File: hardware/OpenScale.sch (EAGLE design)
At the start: 58 parts, among them U1 HX711, U3 TMP102, U4 ATMEGA328P_TQFP, U5 MIC52055-5V, U6 FT231X, Y2 16MHZ

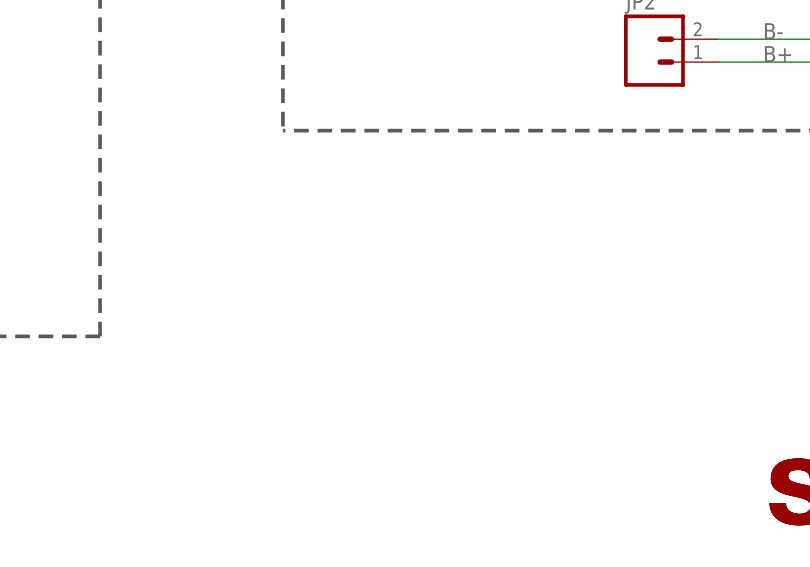
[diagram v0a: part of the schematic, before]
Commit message: Update file names. Remove stat LED blink delay.
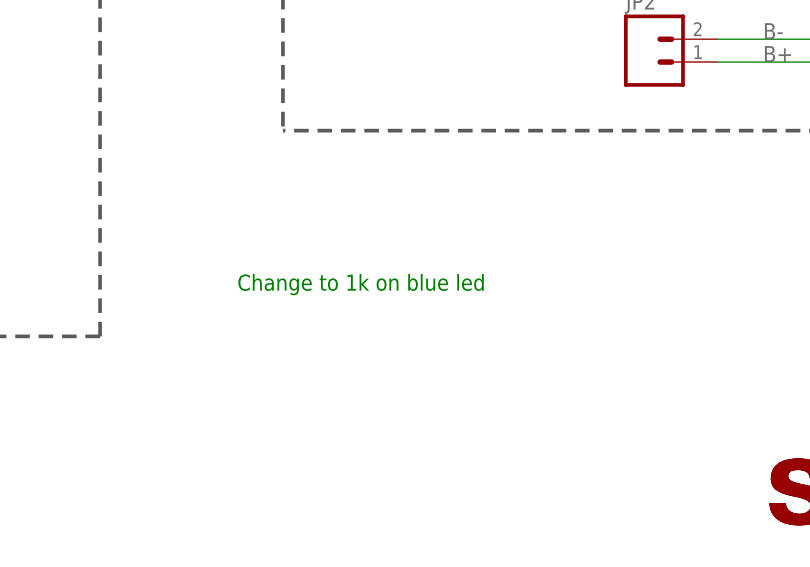
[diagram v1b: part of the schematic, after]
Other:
- note added: "Change to 1k on blue led"
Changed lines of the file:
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@@
 <text x="134.62" y="121.92" size="1.778" layer="97">Optional External
 Serial Interface</text>
+<text x="182.88" y="33.02" size="1.778" layer="91">Change to 1k on blue led</text>
 </plain>
 <instances>

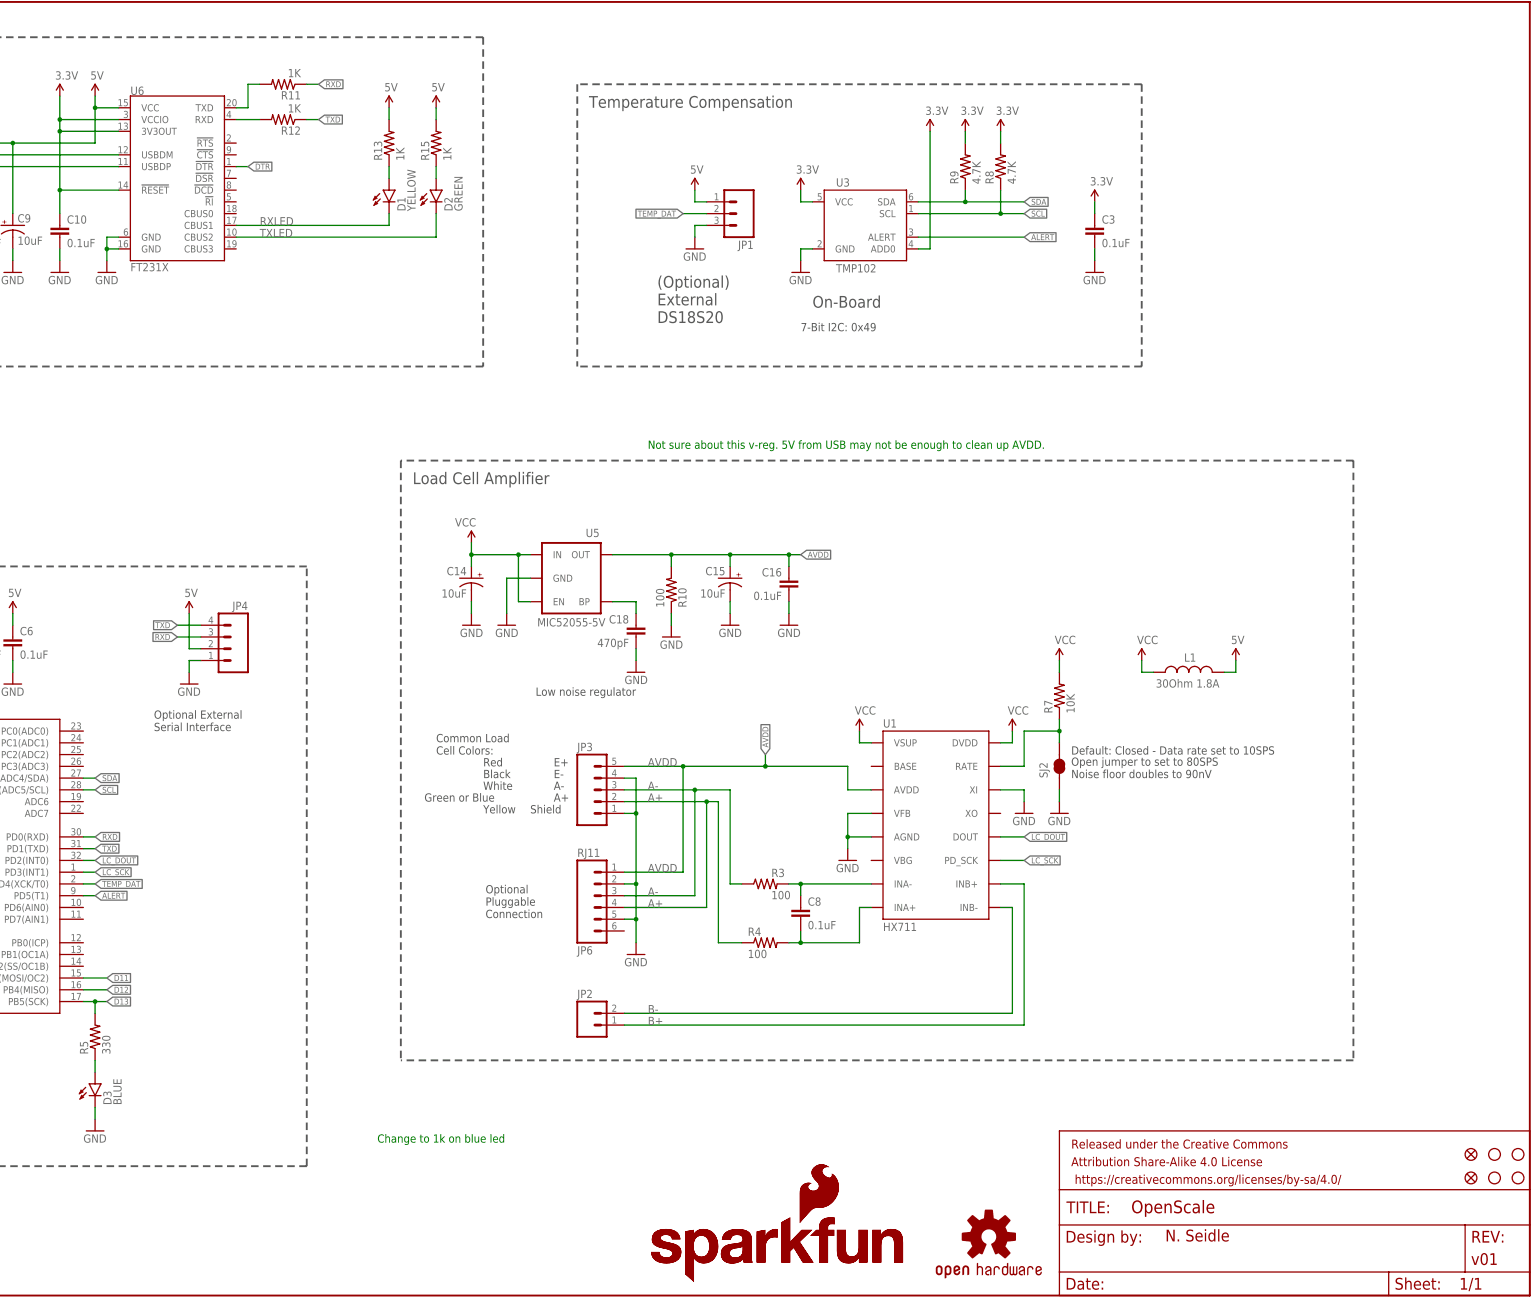
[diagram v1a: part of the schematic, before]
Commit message: Lots of changes. v02 ready for proto.
Changed to RJ45, FTDI connection, MOSFETs to temp sensor, silk, shutdown
from temp sensor to ATmega.
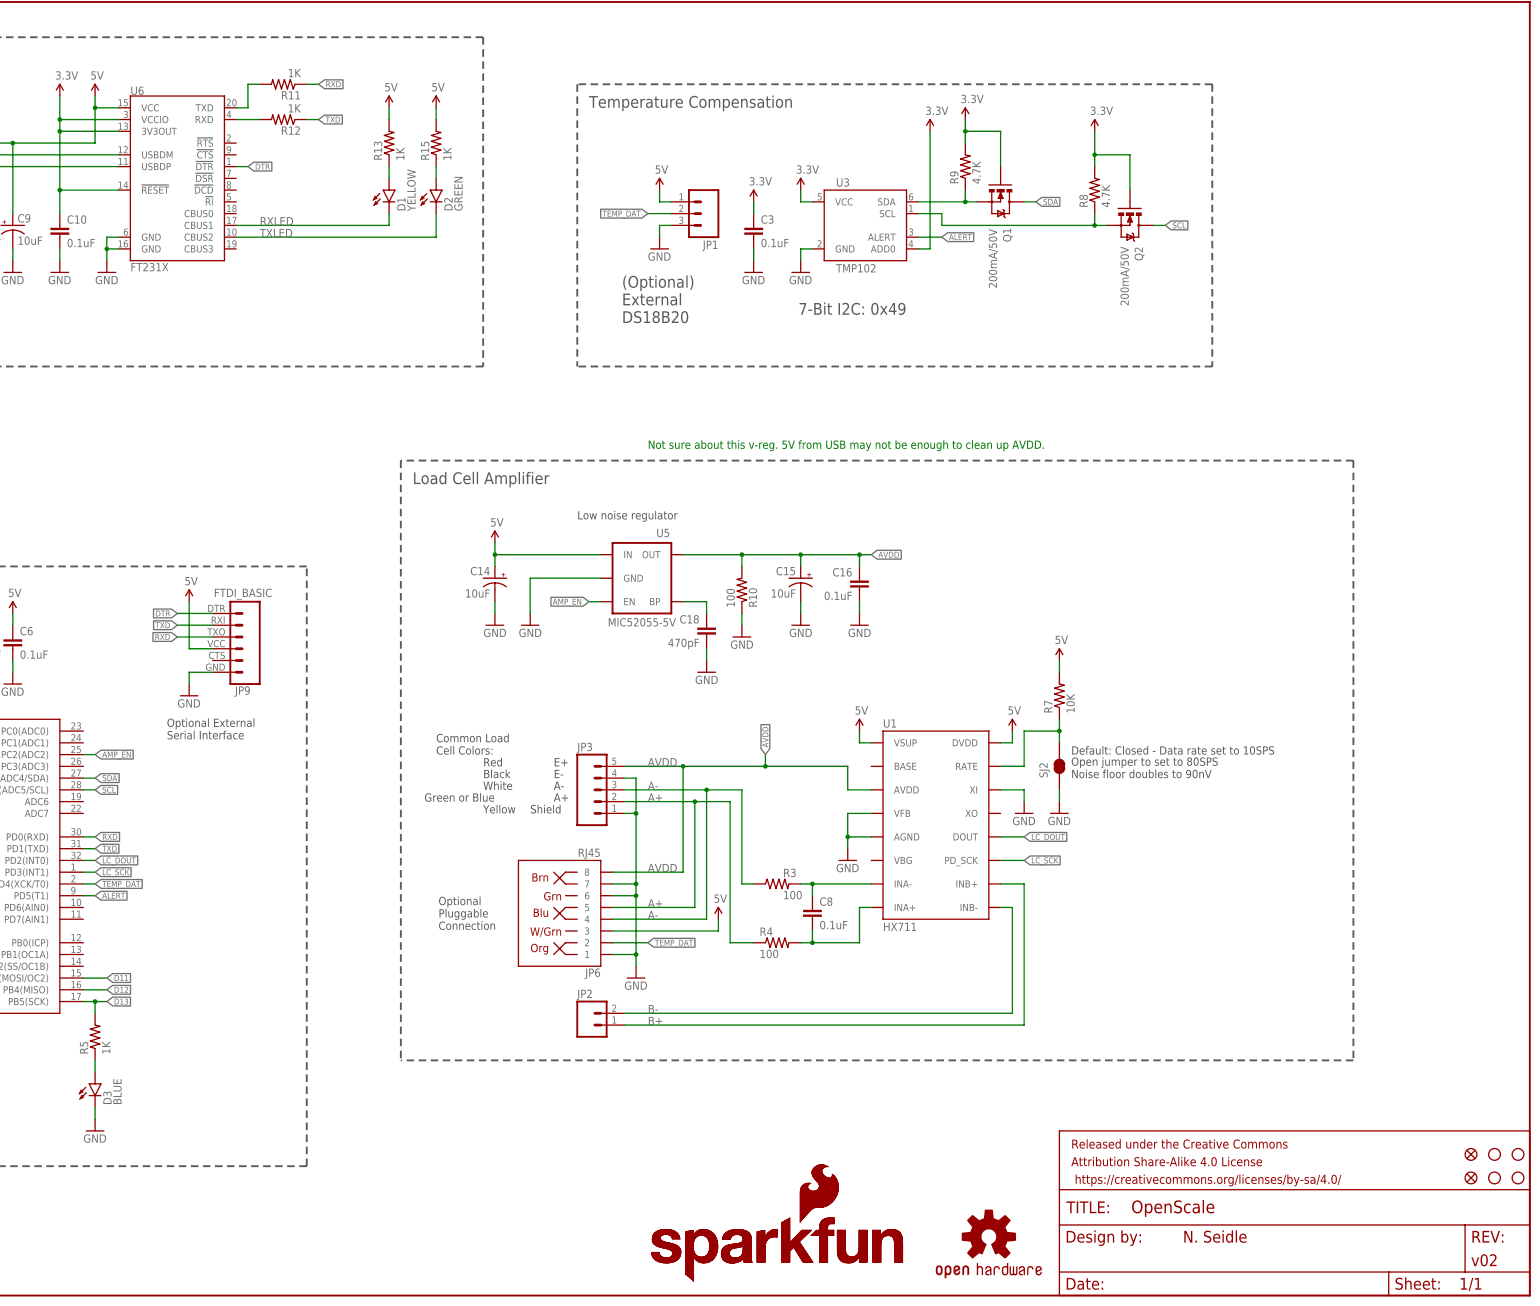
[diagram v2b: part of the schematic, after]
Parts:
- removed JP4: (no value), SparkFun-Connectors:M04PTH
- removed L1: 30Ohm 1.8A, SparkFun-Passives:INDUCTOR30OHM,1.8A
- added JP9: FTDI_BASIC, SparkFun-Connectors:FTDI_BASICPTH
- added Q1, Q2: 200mA/50V, SparkFun-DiscreteSemi:MOSFET-NCHANNELBSS138
- FRAME1: VERSION v01 -> v02
- JP6: value RJ11 -> RJ45; device SparkFun-Connectors:RJ11-6PTH -> SparkFun-Connectors:RJ45-8PTH
- R5: value 330 -> 1K; device SparkFun-Resistors:330OHM1/10W1%(0603) -> SparkFun-Resistors:1KOHM-1/10W-1%(0603)
- S2: device SparkFun-Electromechanical:SWITCH-MOMENTARY-2SMD -> SparkFun-Electromechanical:SWITCH-MOMENTARY-2SMD-1101NE
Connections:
- removed net VCC: C14.+, L1.1, R7.2, U1.DVDD, U1.VSUP, U5.EN, U5.IN
- new net AMP_EN: U4.PC2(ADC2), U5.EN
- new net LV_SCL: Q2.S, R8.1, U3.SCL
- new net LV_SDA: Q1.S, R9.1, U3.SDA
- net 3.3V: now also Q1.G, Q2.G
- net 5V: now also C14.+, JP6.3, JP9.4, R7.2, U1.DVDD, U1.VSUP, U5.IN; no longer JP4.2, L1.2
- net A+: now also JP6.5; no longer JP6.4
- net A-: now also JP6.4; no longer JP6.3
- net AVDD: now also JP6.8; no longer JP6.1
- net DTR: now also JP9.1
- net GND: now also JP6.1, JP6.6, JP6.7, JP9.6; no longer JP4.1, JP6.2, JP6.5
- net RXD: now also JP9.3; no longer JP4.3
- net SCL: now also Q2.D; no longer R8.1, U3.SCL
- net SDA: now also Q1.D; no longer R9.1, U3.SDA
- net TEMP_DAT: now also JP6.2
- net TXD: now also JP9.2; no longer JP4.4
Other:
- note added: "(Optional) External DS18B20"
- note removed: "(Optional) External DS18S20"
- note removed: "Change to 1k on blue led"
- note removed: "On-Board"
- moved on the sheet: C14, C15, C16, C18, C3, C8, JP1, R10, R3, R4, R8, U5

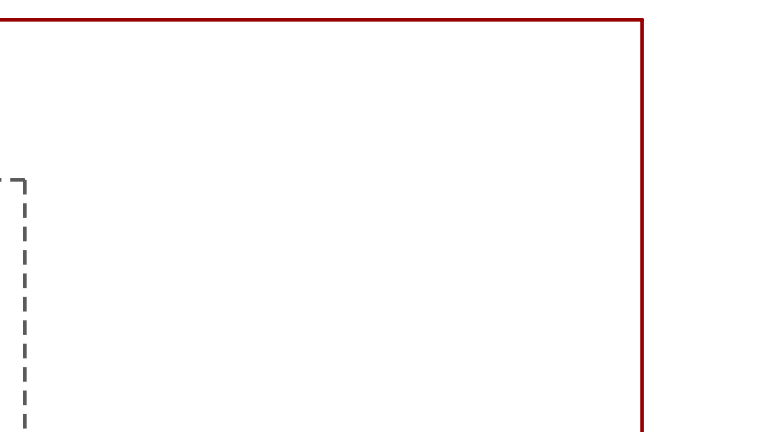
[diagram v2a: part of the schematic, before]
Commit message: Adding support for temperature readings.
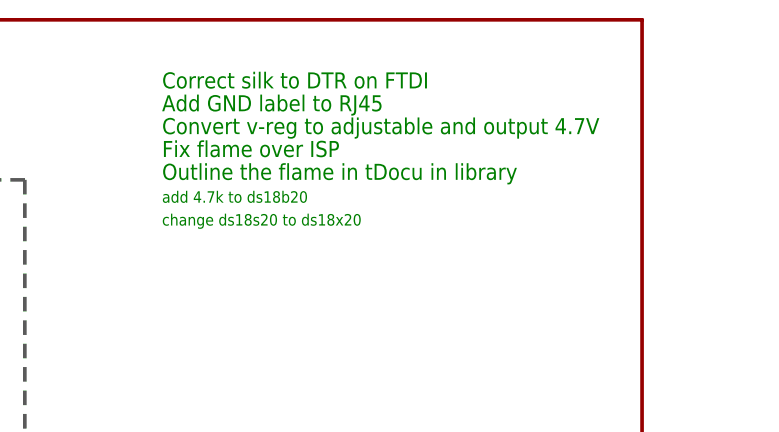
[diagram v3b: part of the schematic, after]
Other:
- note added: "Add GND label to RJ45"
- note added: "Convert v-reg to adjustable and output 4.7V"
- note added: "Correct silk to DTR on FTDI"
- note added: "Fix flame over ISP"
- note added: "Outline the flame in tDocu in library"
- note added: "add 4.7k to ds18b20"
- note added: "change ds18s20 to ds18x20"
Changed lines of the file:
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@@
 <?xml version="1.0" encoding="utf-8"?>
 <!DOCTYPE eagle SYSTEM "eagle.dtd">
-<eagle version="7.1.0">
+<eagle version="7.2.0">
 <drawing>
 <settings>
@@
 <grid distance="0.1" unitdist="inch" unit="inch" style="lines" multiple="1" display="no" altdistance="0.01" altunitdist="inch" altunit="inch"/>
 <layers>
-<layer number="1" name="Top" color="4" fill="1" visible="yes" active="no"/>
-<layer number="2" name="Route2" color="1" fill="3" visible="yes" active="no"/>
-<layer number="3" name="Route3" color="4" fill="3" visible="yes" active="no"/>
-<layer number="4" name="Route4" color="1" fill="4" visible="yes" active="no"/>
-<layer number="5" name="Route5" color="4" fill="4" visible="yes" active="no"/>
-<layer number="6" name="Route6" color="1" fill="8" visible="yes" active="no"/>
-<layer number="7" name="Route7" color="4" fill="8" visible="yes" active="no"/>
-<layer number="8" name="Route8" color="1" fill="2" visible="yes" active="no"/>
-<layer number="9" name="Route9" color="4" fill="2" visible="yes" active="no"/>
-<layer number="10" name="Route10" color="1" fill="7" visible="yes" active="no"/>
-<layer number="11" name="Route11" color="4" fill="7" visible="yes" active="no"/>
-<layer number="12" name="Route12" color="1" fill="5" visible="yes" active="no"/>
-<layer number="13" name="Route13" color="4" fill="5" visible="yes" active="no"/>
-<layer number="14" name="Route14" color="1" fill="6" visible="yes" active="no"/>
-<layer number="15" name="Route15" color="4" fill="6" visible="yes" active="no"/>
-<layer number="16" name="Bottom" color="1" fill="1" visible="yes" active="no"/>
-<layer number="17" name="Pads" color="2" fill="1" visible="yes" active="no"/>
-<layer number="18" name="Vias" color="2" fill="1" visible="yes" active="no"/>
-<layer number="19" name="Unrouted" color="6" fill="1" visible="yes" active="no"/>
-<layer number="20" name="Dimension" color="15" fill="1" visible="yes" active="no"/>
-<layer number="21" name="tPlace" color="16" fill="1" visible="yes" active="no"/>
-<layer number="22" name="bPlace" color="14" fill="1" visible="yes" active="no"/>
-<layer number="23" name="tOrigins" color="15" fill="1" visible="yes" active="no"/>
-<layer number="24" name="bOrigins" color="15" fill="1" visible="yes" active="no"/>
-<layer number="25" name="tNames" color="7" fill="1" visible="yes" active="no"/>
-<layer number="26" name="bNames" color="7" fill="1" visible="yes" active="no"/>
-<layer number="27" name="tValues" color="7" fill="1" visible="yes" active="no"/>
-<layer number="28" name="bValues" color="7" fill="1" visible="yes" active="no"/>
+<layer number="1" name="Top" color="4" fill="1" visible="no" active="no"/>
+<layer number="2" name="Route2" color="1" fill="3" visible="no" active="no"/>
+<layer number="3" name="Route3" color="4" fill="3" visible="no" active="no"/>
+<layer number="4" name="Route4" color="1" fill="4" visible="no" active="no"/>
+<layer number="5" name="Route5" color="4" fill="4" visible="no" active="no"/>
+<layer number="6" name="Route6" color="1" fill="8" visible="no" active="no"/>
+<layer number="7" name="Route7" color="4" fill="8" visible="no" active="no"/>
+<layer number="8" name="Route8" color="1" fill="2" visible="no" active="no"/>
+<layer number="9" name="Route9" color="4" fill="2" visible="no" active="no"/>
+<layer number="10" name="Route10" color="1" fill="7" visible="no" active="no"/>
+<layer number="11" name="Route11" color="4" fill="7" visible="no" active="no"/>
+<layer number="12" name="Route12" color="1" fill="5" visible="no" active="no"/>
+<layer number="13" name="Route13" color="4" fill="5" visible="no" active="no"/>
+<layer number="14" name="Route14" color="1" fill="6" visible="no" active="no"/>
+<layer number="15" name="Route15" color="4" fill="6" visible="no" active="no"/>
+<layer number="16" name="Bottom" color="1" fill="1" visible="no" active="no"/>
+<layer number="17" name="Pads" color="2" fill="1" visible="no" active="no"/>
+<layer number="18" name="Vias" color="2" fill="1" visible="no" active="no"/>
+<layer number="19" name="Unrouted" color="6" fill="1" visible="no" active="no"/>
+<layer number="20" name="Dimension" color="15" fill="1" visible="no" active="no"/>
+<layer number="21" name="tPlace" color="16" fill="1" visible="no" active="no"/>
+<layer number="22" name="bPlace" color="14" fill="1" visible="no" active="no"/>
+<layer number="23" name="tOrigins" color="15" fill="1" visible="no" active="no"/>
+<layer number="24" name="bOrigins" color="15" fill="1" visible="no" active="no"/>
+<layer number="25" name="tNames" color="7" fill="1" visible="no" active="no"/>
+<layer number="26" name="bNames" color="7" fill="1" visible="no" active="no"/>
+<layer number="27" name="tValues" color="7" fill="1" visible="no" active="no"/>
+<layer number="28" name="bValues" color="7" fill="1" visible="no" active="no"/>
 <layer number="29" name="tStop" color="5" fill="1" visible="no" active="no"/>
 <layer number="30" name="bStop" color="7" fill="6" visible="no" active="no"/>
@@
 <layer number="35" name="tGlue" color="7" fill="4" visible="no" active="no"/>
 <layer number="36" name="bGlue" color="7" fill="5" visible="no" active="no"/>
-<layer number="37" name="tTest" color="7" fill="1" visible="yes" active="no"/>
-<layer number="38" name="bTest" color="7" fill="1" visible="yes" active="no"/>
+<layer number="37" name="tTest" color="7" fill="1" visible="no" active="no"/>
+<layer number="38" name="bTest" color="7" fill="1" visible="no" active="no"/>
 <layer number="39" name="tKeepout" color="4" fill="11" visible="no" active="no"/>
 <layer number="40" name="bKeepout" color="1" fill="11" visible="no" active="no"/>
@@
 <layer number="44" name="Drills" color="7" fill="1" visible="no" active="no"/>
 <layer number="45" name="Holes" color="7" fill="1" visible="no" active="no"/>
-<layer number="46" name="Milling" color="3" fill="1" visible="yes" active="no"/>
-<layer number="47" name="Measures" color="7" fill="1" visible="yes" active="no"/>
-<layer number="48" name="Document" color="7" fill="1" visible="yes" active="no"/>
-<layer number="49" name="Reference" color="7" fill="1" visible="yes" active="no"/>
-<layer number="50" name="dxf" color="7" fill="1" visible="yes" active="no"/>
-<layer number="51" name="tDocu" color="6" fill="1" visible="yes" active="no"/>
-<layer number="52" name="bDocu" color="7" fill="1" visible="yes" active="no"/>
-<layer number="53" name="tGND_GNDA" color="7" fill="9" visible="yes" active="no"/>
-<layer number="54" name="bGND_GNDA" color="1" fill="9" visible="yes" active="no"/>
-<layer number="56" name="wert" color="7" fill="1" visible="yes" active="no"/>
-<layer number="57" name="tCAD" color="7" fill="1" visible="yes" active="no"/>
-<layer number="59" name="tCarbon" color="7" fill="1" visible="yes" active="no"/>
-<layer number="60" name="bCarbon" color="7" fill="1" visible="yes" active="no"/>
+<layer number="46" name="Milling" color="3" fill="1" visible="no" active="no"/>
+<layer number="47" name="Measures" color="7" fill="1" visible="no" active="no"/>
+<layer number="48" name="Document" color="7" fill="1" visible="no" active="no"/>
+<layer number="49" name="Reference" color="7" fill="1" visible="no" active="no"/>
+<layer number="50" name="dxf" color="7" fill="1" visible="no" active="no"/>
+<layer number="51" name="tDocu" color="6" fill="1" visible="no" active="no"/>
+<layer number="52" name="bDocu" color="7" fill="1" visible="no" active="no"/>
+<layer number="53" name="tGND_GNDA" color="7" fill="9" visible="no" active="no"/>
+<layer number="54" name="bGND_GNDA" color="1" fill="9" visible="no" active="no"/>
+<layer number="56" name="wert" color="7" fill="1" visible="no" active="no"/>
+<layer number="57" name="tCAD" color="7" fill="1" visible="no" active="no"/>
+<layer number="59" name="tCarbon" color="7" fill="1" visible="no" active="no"/>
+<layer number="60" name="bCarbon" color="7" fill="1" visible="no" active="no"/>
 <layer number="90" name="Modules" color="5" fill="1" visible="yes" active="yes"/>
 <layer number="91" name="Nets" color="2" fill="1" visible="yes" active="yes"/>
@@
 <text x="137.414" y="120.142" size="1.778" layer="97">Optional External
 Serial Interface</text>
+<text x="378.46" y="271.78" size="1.778" layer="91">Correct silk to DTR on FTDI</text>
+<text x="378.46" y="269.24" size="1.778" layer="91">Add GND label to RJ45</text>
+<text x="378.46" y="266.7" size="1.778" layer="91">Convert v-reg to adjustable and output 4.7V</text>
+<text x="378.46" y="264.16" size="1.778" layer="91">Fix flame over ISP</text>
+<text x="378.46" y="261.62" size="1.778" layer="91">Outline the flame in tDocu in library</text>
+<text x="378.46" y="259.08" size="1.27" layer="91">add 4.7k to ds18b20</text>
+<text x="378.46" y="256.54" size="1.27" layer="91">change ds18s20 to ds18x20</text>
 </plain>
 <instances>
